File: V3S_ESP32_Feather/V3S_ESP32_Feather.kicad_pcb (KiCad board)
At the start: 2 copper layers, 30.5 x 48.3 mm, 81 parts, among them J1 USB_B_Micro, J10 UART, J2 PWM, J3 CAM, J4 I2C, J5 U.FL-R-SMT(01), J7 Micro_SD_Card_Det, J9 I2C, U1 V3S, U2 ADP322ACPZ-145-R7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

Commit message: almost everything is routed !
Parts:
- added C17: 10uF, Capacitor_SMD:C_0201_0603Metric, F.Cu at (36.3, 38.6)
- C12, C2, R13: moved to B.Cu
- C43, C44, C45, C46, C48, C49, R6: moved to F.Cu
- moved C54 36.7 mm to (33.0, 49.9), turned to 90 degrees
- moved D1 34.2 mm to (52.1, 33.0), turned to 270 degrees
- moved C2 32.2 mm to (31.6, 23.7), turned to 180 degrees
- moved D2 28.7 mm to (37.6, 22.5), turned to 270 degrees
- moved C56 25.7 mm to (43.7, 48.3), turned to 180 degrees
- moved C61 25.7 mm to (43.7, 45.5), turned to 0 degrees
- moved C46 24.1 mm to (40.4, 49.8), turned to 90 degrees
- moved C44 21.9 mm to (43.7, 43.1), turned to 180 degrees
- moved R7 18.2 mm to (38.6, 25.3), turned to 270 degrees
- moved C48 16.1 mm to (32.4, 44.5)
- moved C49 15.4 mm to (27.9, 38.0), turned to 180 degrees
- moved C43 14.5 mm to (27.9, 39.2), turned to 180 degrees
- moved C45 10.6 mm to (37.3, 38.5), turned to 270 degrees
- moved R13 10.6 mm to (36.1, 26.7), turned to 0 degrees
- moved C57 10.4 mm to (43.3, 19.1)
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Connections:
- C61 pad 2: +3V3 -> +3V0
- J3 pad 1: /All V3s input output/STROBE -> (no net)
- J3 pad 10: Net-(J3-Pad10) -> (no net)
- J7 pad 10: Net-(J7-Pad10) -> (no net)
- J7 pad 9: Net-(J7-Pad9) -> (no net)
- U1 pad 10: Net-(U1-Pad10) -> (no net)
- U1 pad 11: Net-(U1-Pad11) -> (no net)
- U1 pad 112: Net-(U1-Pad112) -> (no net)
- U1 pad 113: Net-(U1-Pad113) -> (no net)
- U1 pad 114: Net-(U1-Pad114) -> (no net)
- U1 pad 12: /PMIC Power Battery/VCC_PE -> +3V3
- U1 pad 120: Net-(U1-Pad120) -> (no net)
- U1 pad 121: Net-(U1-Pad121) -> (no net)
- U1 pad 124: Net-(U1-Pad124) -> (no net)
- U1 pad 125: Net-(U1-Pad125) -> (no net)
- U1 pad 13: Net-(U1-Pad13) -> (no net)
- U1 pad 14: Net-(U1-Pad14) -> (no net)
- U1 pad 29: /PMIC Power Battery/VCC_PE -> +3V3
- U1 pad 43: Net-(U1-Pad43) -> (no net)
- U1 pad 44: Net-(U1-Pad44) -> (no net)
- U1 pad 52: Net-(U1-Pad52) -> (no net)
- U1 pad 53: Net-(U1-Pad53) -> (no net)
- U1 pad 54: Net-(U1-Pad54) -> (no net)
- U1 pad 55: Net-(U1-Pad55) -> (no net)
- U1 pad 6: Net-(U1-Pad6) -> (no net)
- U1 pad 7: Net-(U1-Pad7) -> (no net)
- U1 pad 77: Net-(U1-Pad77) -> (no net)
- U1 pad 78: Net-(U1-Pad78) -> (no net)
- U1 pad 81: Net-(U1-Pad81) -> (no net)
- U1 pad 82: Net-(U1-Pad82) -> (no net)
- U1 pad 83: Net-(U1-Pad83) -> (no net)
- U1 pad 84: Net-(U1-Pad84) -> (no net)
- U1 pad 86: Net-(U1-Pad86) -> (no net)
- U1 pad 87: Net-(U1-Pad87) -> (no net)
- U1 pad 89: Net-(U1-Pad89) -> (no net)
- U1 pad 90: Net-(U1-Pad90) -> (no net)
- U1 pad 91: Net-(U1-Pad91) -> (no net)
- U1 pad 92: Net-(U1-Pad92) -> (no net)
- U2 pad 4: Net-(U2-Pad4) -> (no net)
- U2 pad 7: Net-(U2-Pad7) -> (no net)
- U3 pad 14: Net-(U3-Pad14) -> (no net)
- U3 pad 15: Net-(U3-Pad15) -> (no net)
- U3 pad 16: Net-(U3-Pad16) -> (no net)
- U3 pad 17: Net-(U3-Pad17) -> (no net)
- U3 pad 19: Net-(U3-Pad19) -> (no net)
- U3 pad 2: Net-(U3-Pad2) -> (no net)
- U3 pad 21: Net-(U3-Pad21) -> (no net)
- U3 pad 3: Net-(U3-Pad3) -> (no net)
- U3 pad 4: Net-(U3-Pad4) -> (no net)
- U3 pad 5: Net-(U3-Pad5) -> (no net)
- U3 pad 6: Net-(U3-Pad6) -> (no net)
- U3 pad 7: Net-(U3-Pad7) -> (no net)
- U5 pad 25: Net-(U5-Pad25) -> (no net)
- U5 pad 26: Net-(U5-Pad26) -> (no net)
- U5 pad 27: Net-(U5-Pad27) -> (no net)
- U5 pad 28: /WIFI, BT, RT/SD2 -> (no net)
- U5 pad 29: /WIFI, BT, RT/SD3 -> (no net)
- U5 pad 30: Net-(U5-Pad30) -> (no net)
- U5 pad 31: Net-(U5-Pad31) -> (no net)
- U5 pad 32: Net-(U5-Pad32) -> (no net)
- U5 pad 33: Net-(U5-Pad33) -> (no net)
- U5 pad 5: Net-(U5-Pad5) -> (no net)
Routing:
- net /WIFI, BT, RT/UART0_RX: track 1.36 -> 36.7 mm, vias 0 -> 3
- net /WIFI, BT, RT/UART0_TX: track 7.88 -> 35.5 mm, vias 0 -> 3
- net +3V3: track 26.8 -> 51.2 mm, vias 2 -> 9
- net +3V0: track 11.8 -> 35.0 mm, vias 0 -> 3
- net GND: track 0.00 -> 17.3 mm, vias 0 -> 1
- net +1V8: track 21.0 -> 36.1 mm, vias 1 -> 4
- net /PMIC Power Battery/VIN: track 9.16 -> 24.1 mm, vias 0 -> 1
- net /WIFI, BT, RT/ICM_INT: track 0.00 -> 13.5 mm, vias 0 -> 2
- net /WIFI, BT, RT/IO0: track 6.40 -> 15.3 mm, vias 1 -> 2
- net VBUS: track 4.38 -> 11.4 mm
- net +BATT: track 0.00 -> 6.72 mm
- net /WIFI, BT, RT/SCL: track 13.2 -> 18.7 mm
- net /WIFI, BT, RT/MOSI: track 10.2 -> 14.7 mm
- net +1V2: track 5.73 -> 1.56 mm
- net Net-(R8-Pad1): track 0.00 -> 3.47 mm
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
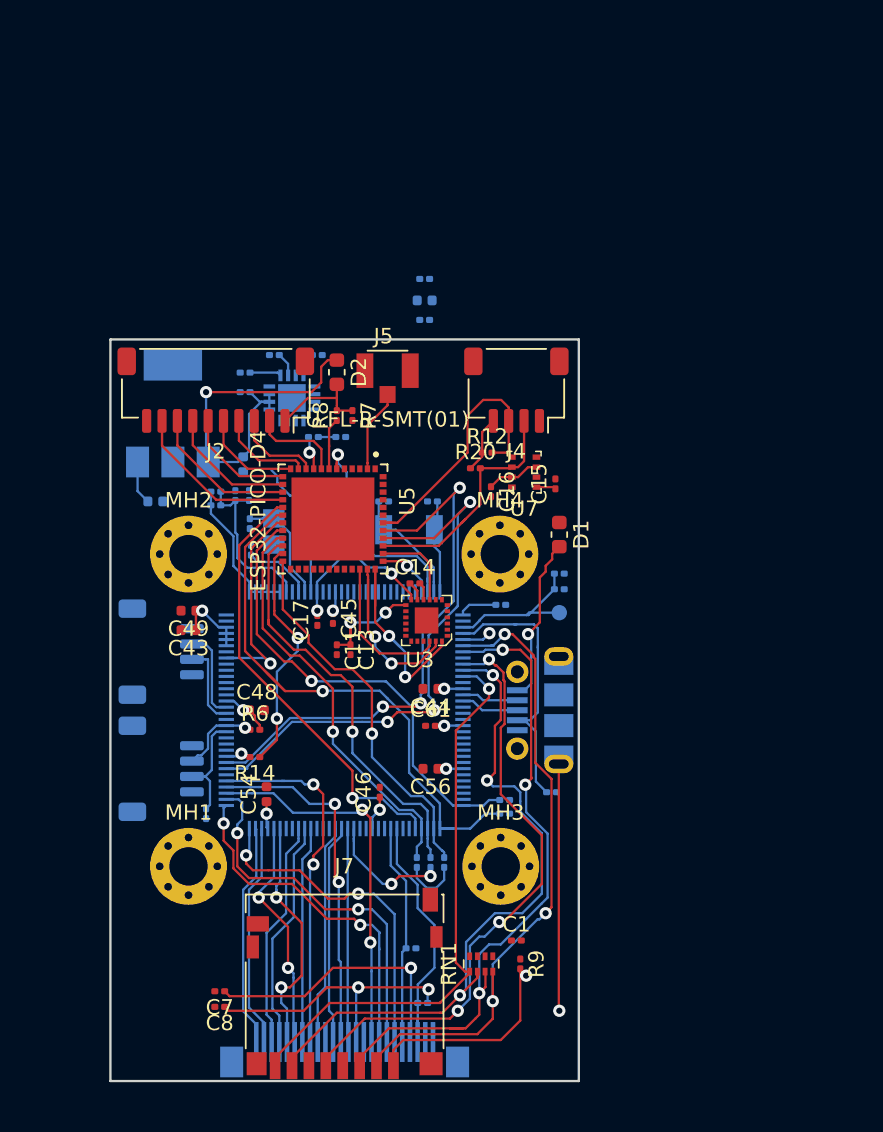
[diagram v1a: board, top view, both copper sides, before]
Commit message: SD card connector re routed, only power remaining
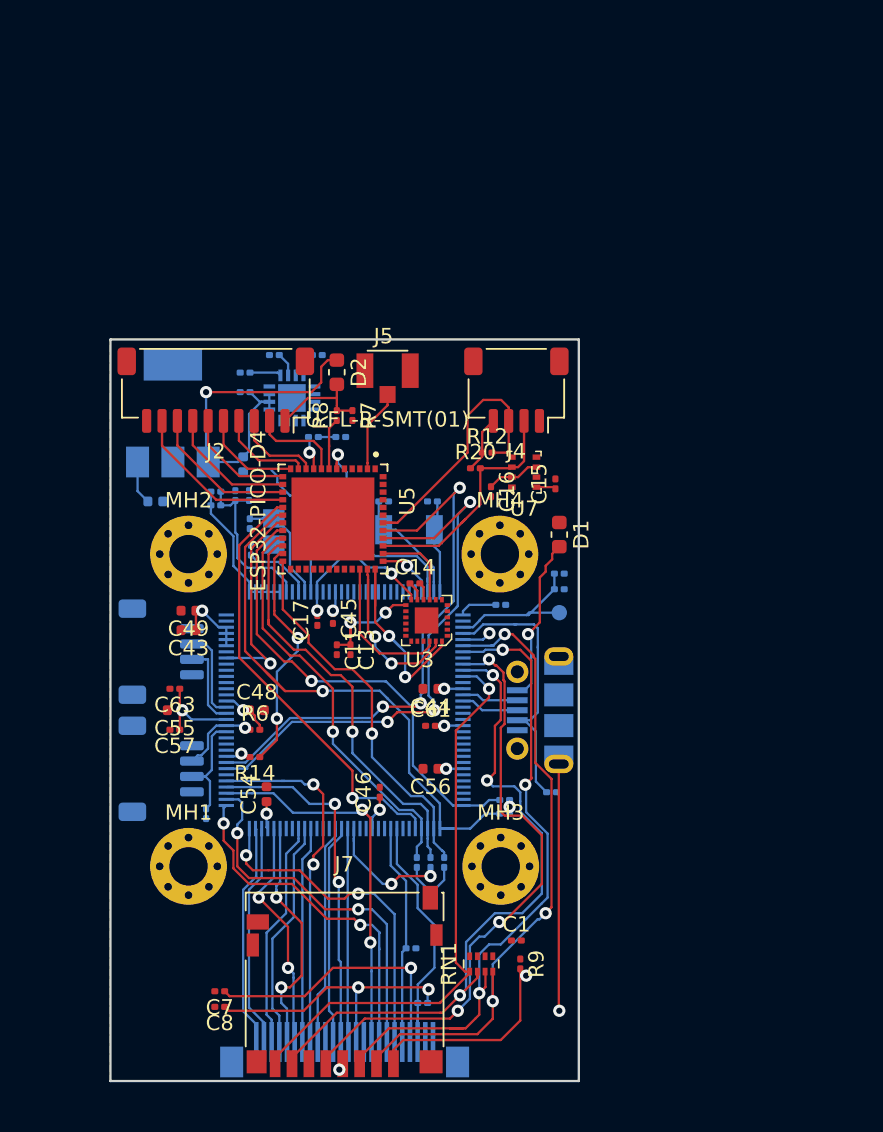
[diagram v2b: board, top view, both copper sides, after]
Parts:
- C55, C57, C63: moved to F.Cu
- moved C55 31.2 mm to (27.1, 44.5), turned to 180 degrees
- moved C57 31.2 mm to (27.1, 45.7), turned to 180 degrees
- moved C63 31.2 mm to (27.1, 43.1), turned to 180 degrees
- moved J7 0.13 mm to (38.1, 62.1)
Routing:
- net +1V2: track 1.56 -> 7.34 mm, vias 0 -> 1
- net +3V3: track 51.2 -> 53.0 mm, vias 9 -> 11
- net /All V3s input output/PF2: track 39.4 -> 40.1 mm

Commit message: Power part autorouted, replaced micro usb connector by jst sh 5 pin
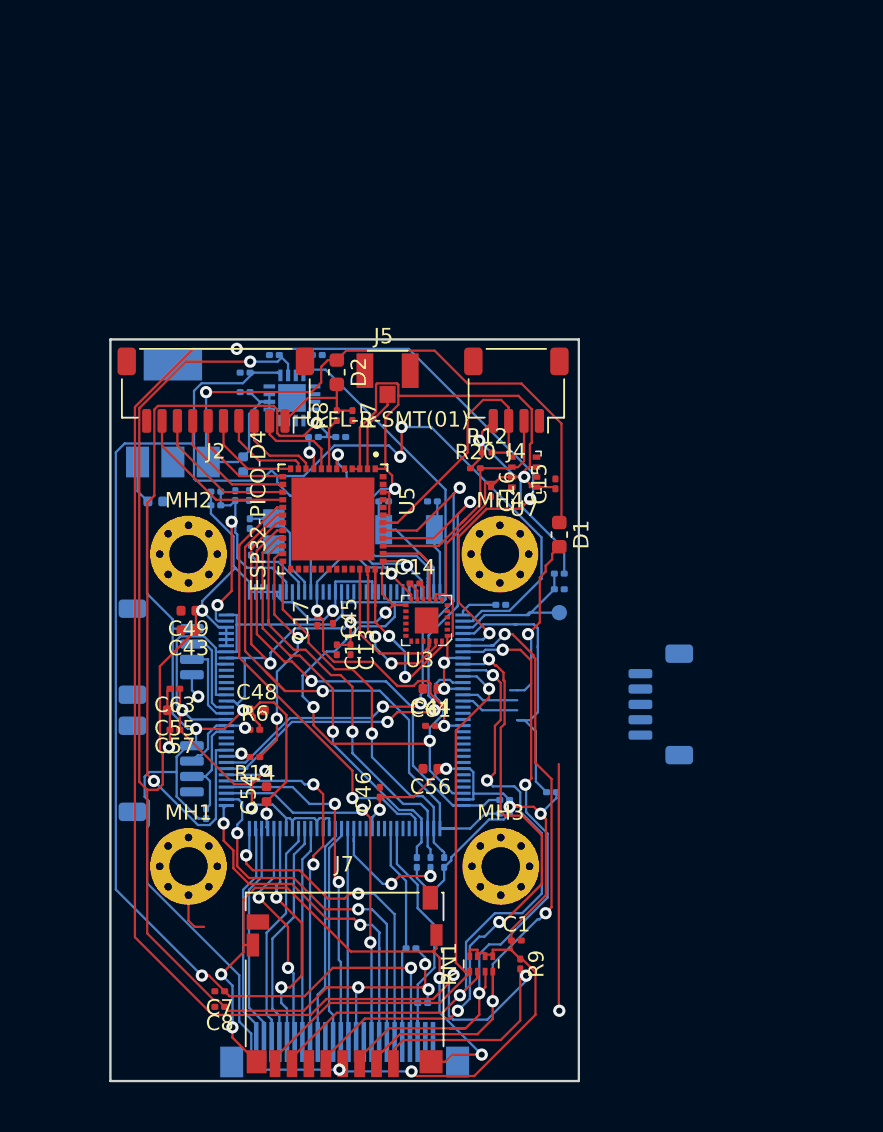
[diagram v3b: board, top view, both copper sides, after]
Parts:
- J1: footprint Connector_USB:USB_Micro-B_Molex-105017-0001 -> Connector_JST:JST_SH_BM05B-SRSS-TB_1x05-1MP_P1.00mm_Vertical
- moved J1 7.88 mm to (58.7, 44.1), turned to 90 degrees
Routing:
- net +3V3: track 53.0 -> 260.0 mm, vias 11 -> 18
- net /All V3s input output/PF5: track 15.9 -> 129.1 mm, vias 2 -> 5
- net +3V0: track 35.0 -> 140.1 mm, vias 3 -> 6
- net +1V2: track 7.34 -> 111.4 mm, vias 1 -> 5
- net +1V8: track 36.1 -> 116.1 mm, vias 4 -> 6
- net /WIFI, BT, RT/EN: track 1.14 -> 50.1 mm, vias 0 -> 2
- net Net-(J7-Pad11): track 0.00 -> 39.8 mm, vias 0 -> 4
- net /PMIC Power Battery/VIN: track 24.1 -> 47.4 mm
- net GND: track 17.3 -> 27.6 mm, vias 1 -> 3
- net /PMIC Power Battery/SVREF: track 11.1 -> 19.0 mm, vias 0 -> 2

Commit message: progress on pcb cleaning
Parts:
- J1: value USB_B_Micro -> USB_Micro
- moved J1 7.87 mm to (50.8, 44.1)
- moved C54 1.89 mm to (34.4, 51.2), turned to 0 degrees
- moved R30 1.73 mm to (40.6, 34.3), turned to 0 degrees
- moved C17 1.59 mm to (35.9, 37.1), turned to 0 degrees
- moved C48 1.55 mm to (31.5, 43.2), turned to 180 degrees
- moved C5 1.53 mm to (31.4, 26.9), turned to 90 degrees
- moved C45 1.45 mm to (37.7, 37.1), turned to 0 degrees
- moved C41 1.02 mm to (41.7, 30.7), turned to 0 degrees
- moved C11 0.99 mm to (38.2, 39.8), turned to 180 degrees
- moved C4 0.80 mm to (47.5, 37.6)
- moved C16 0.57 mm to (47.9, 29.7)
- moved C13 0.28 mm to (38.2, 40.6), turned to 180 degrees
- moved Y2 0.19 mm to (42.3, 32.5)
- moved C40 0.13 mm to (43.8, 30.7)
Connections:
- J1 pad 1: VBUS -> GND
- J1 pad 2: /USB_D_N -> /USB_D_P
- J1 pad 3: /USB_D_P -> /USB_D_N
- J1 pad 4: /USB_ID -> VBUS
- J1 pad 5: GND -> /USB_ID
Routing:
- net GND: track 27.6 -> 101.2 mm, vias 3 -> 27
- net +3V3: track 260.0 -> 264.5 mm
- net +3V0: track 140.1 -> 142.4 mm
- net Net-(R30-Pad2): track 6.52 -> 4.60 mm
- net +1V8: track 116.1 -> 117.6 mm
- net Net-(C41-Pad2): track 8.10 -> 9.32 mm
- net /All V3s input output/PF5: track 129.1 -> 130.3 mm
- net /All V3s input output/PF3: track 42.9 -> 41.8 mm
- net Net-(C4-Pad2): track 2.56 -> 1.74 mm
- net /All V3s input output/SDIO1_DAT3: track 30.5 -> 31.0 mm
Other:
- board size 30.5 x 48.3 mm -> 30.5 x 50.8 mm

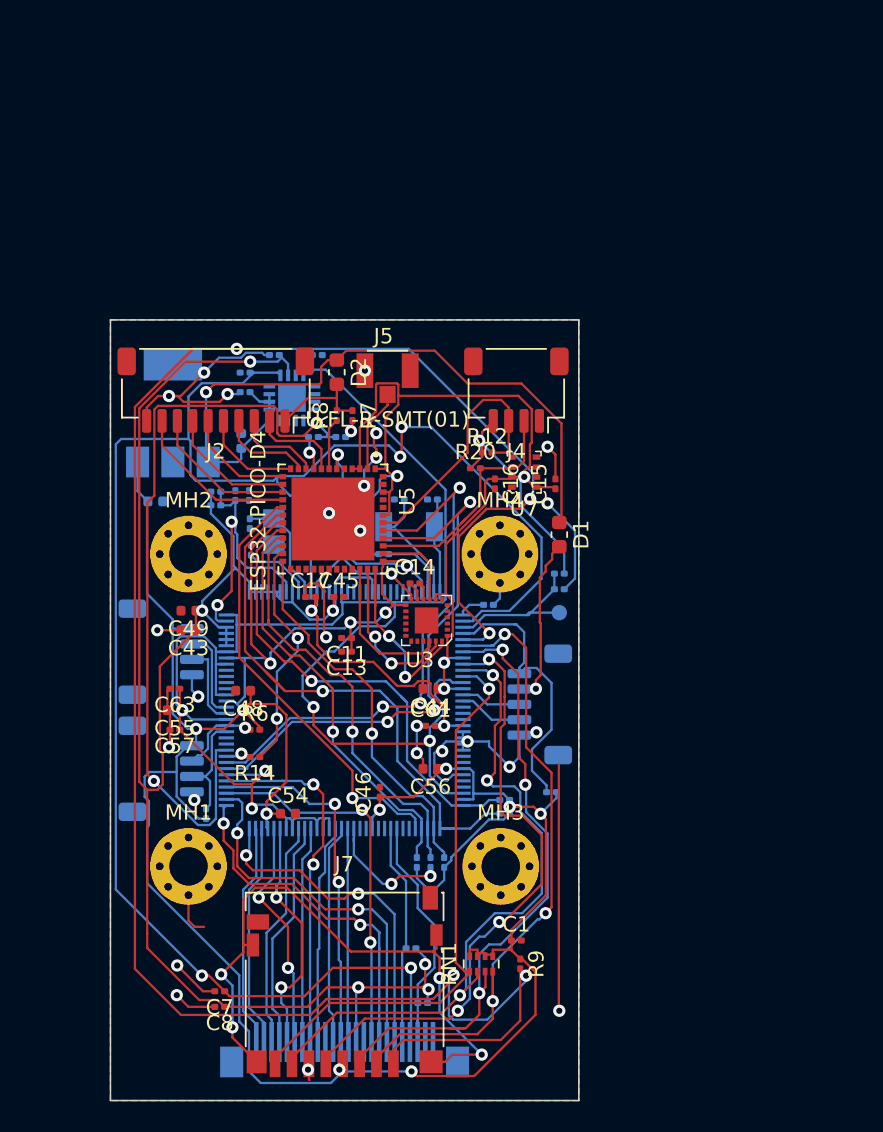
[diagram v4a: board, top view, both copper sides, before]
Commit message: cleaner sdcard routing, bom exported (need price and url)
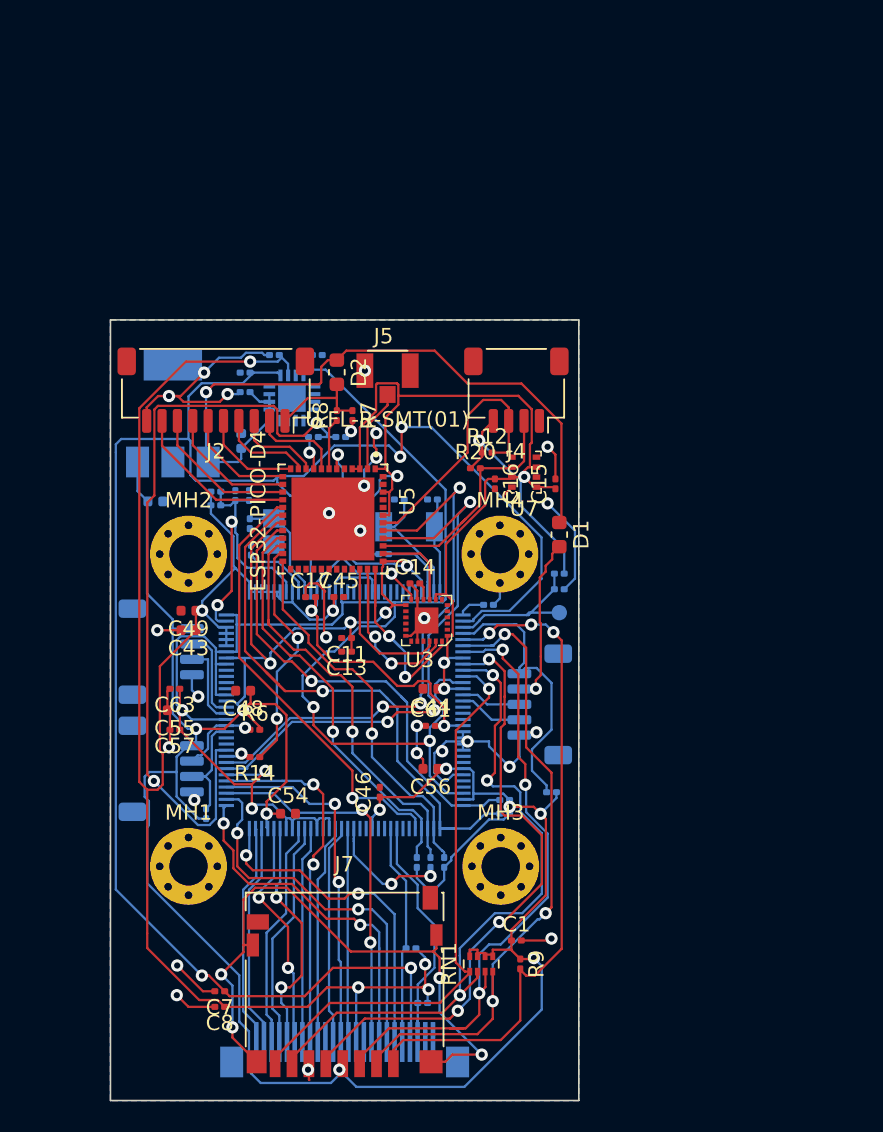
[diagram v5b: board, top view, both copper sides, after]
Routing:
- net /All V3s input output/PF5: track 130.3 -> 44.4 mm, vias 5 -> 3
- net GND: track 101.2 -> 87.6 mm, vias 27 -> 28
- net +3V3: track 264.5 -> 266.3 mm

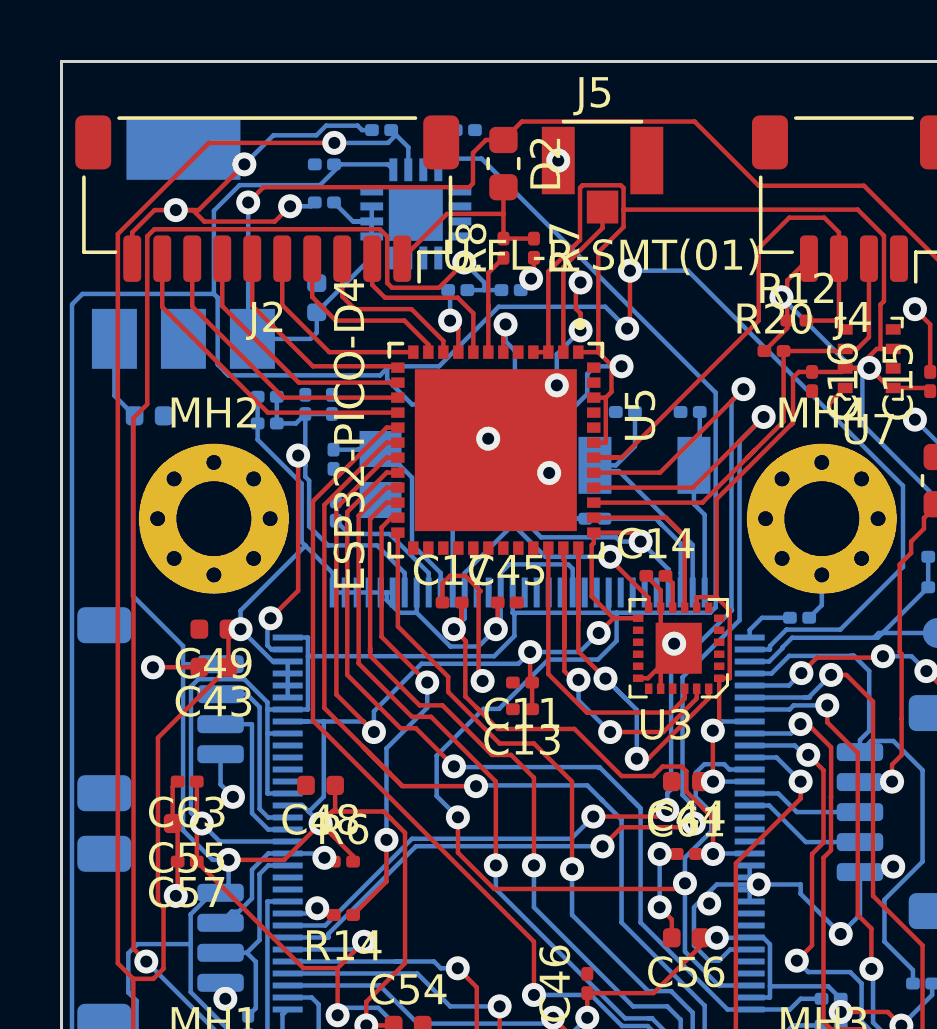
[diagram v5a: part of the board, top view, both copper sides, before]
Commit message: 3 ground issues fixed
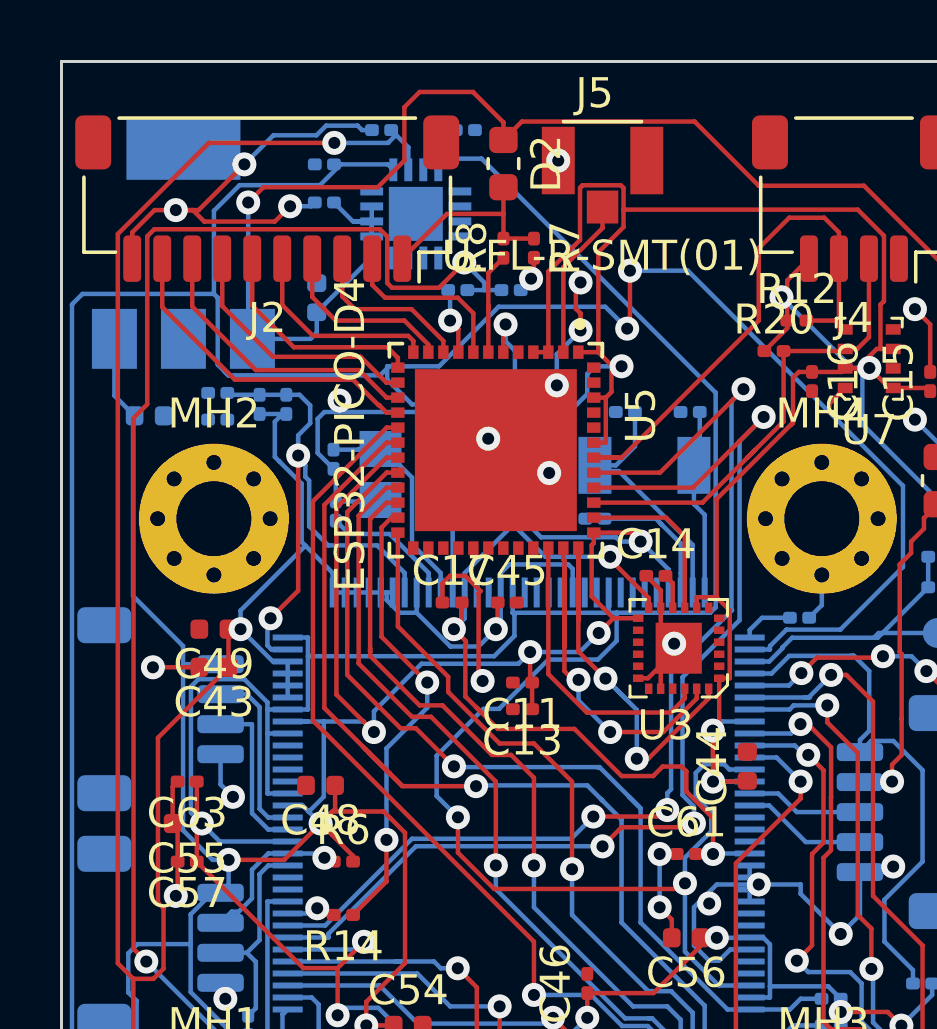
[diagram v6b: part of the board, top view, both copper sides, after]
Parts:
- moved C65 3.83 mm to (28.1, 30.1), turned to 0 degrees
- moved R32 2.96 mm to (28.1, 31.0), turned to 0 degrees
- moved C44 2.09 mm to (45.7, 42.5), turned to 90 degrees
- moved C64 0.90 mm to (30.4, 30.5), turned to 270 degrees
- moved R31 0.36 mm to (29.5, 30.5), turned to 270 degrees
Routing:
- net GND: track 87.6 -> 96.4 mm, vias 28 -> 29
- net /PMIC Power Battery/VIN: track 47.5 -> 49.6 mm
- net /PMIC Power Battery/SVREF: track 19.0 -> 20.0 mm
- net +3V3: track 266.3 -> 267.1 mm
